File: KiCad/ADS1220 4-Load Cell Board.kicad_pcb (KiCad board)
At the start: 2 copper layers, 101.6 x 50.8 mm, 75 parts, among them J1 Conn_01x04, J2 Conn_01x04, J3 Conn_01x04, J4 Conn_ARM_SWD_TagConnect_TC203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, J5 USB_C_Receptacle_USB2.0_14P, J7 Conn_01x04, SW1 SW_Push, SW2 SW_Push, U1 STM32F103C8Tx, U2 ADS1220xPW, U3 MCP6V92-E/MS, U4 NCP1117-3.3_SOT223, U6 TLV702475_SOT23-5, Y1 8Mhz

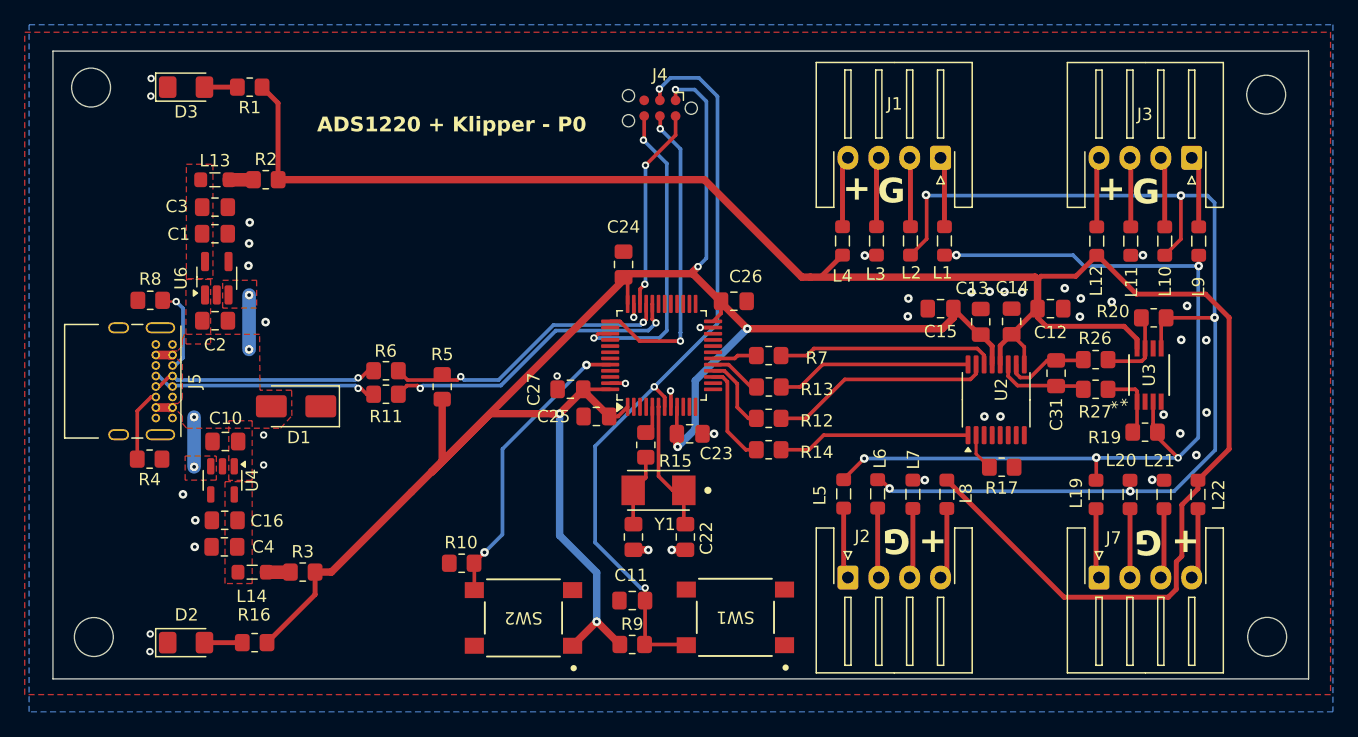
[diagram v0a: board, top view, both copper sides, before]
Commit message: Re-add Via Stitching
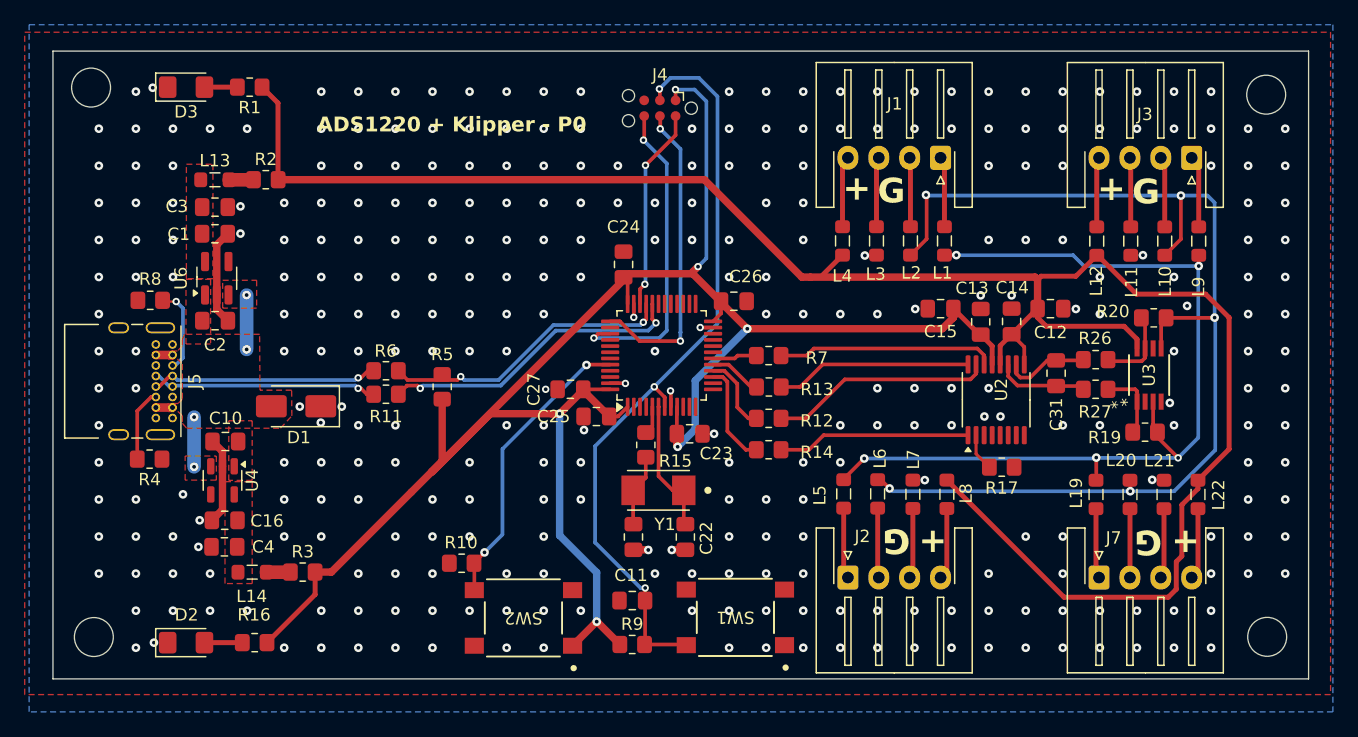
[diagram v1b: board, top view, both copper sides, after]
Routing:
- net GND: track 7.00 -> 21.8 mm, vias 44 -> 327

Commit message: Work In Progress
moving towards v 2
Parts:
- removed J4: Conn_ARM_SWD_TagConnect_TC2030-NL, Connector:Tag-Connect_TC2030-IDC-NL_2x03_P1.27mm_Vertical
- removed SW1, SW2: SW_Push, PTS645 Switch:SWITCH_43SMTR92LFS
- added C5: 10uF, Capacitor_SMD:C_0805_2012Metric_Pad1.18x1.45mm_HandSolder, F.Cu at (116.2, 100.2)
- added C6: 10uF, Capacitor_SMD:C_0805_2012Metric_Pad1.18x1.45mm_HandSolder, F.Cu at (114.2, 100.2)
- added C7: 0.1uF, Capacitor_SMD:C_0805_2012Metric_Pad1.18x1.45mm_HandSolder, F.Cu at (117.3, 95.9)
- added C8: 0.1uF, Capacitor_SMD:C_0805_2012Metric_Pad1.18x1.45mm_HandSolder, F.Cu at (117.3, 89.9)
- added D4: LED, LED_SMD:LED_1206_3216Metric_Pad1.42x1.75mm_HandSolder, F.Cu at (95.0, 72.3)
- added J6: Conn_01x02, Connector_PinHeader_2.54mm:PinHeader_1x02_P2.54mm_Vertical, F.Cu at (91.8, 116.9)
- added J8: Conn_01x02, Connector_PinHeader_2.54mm:PinHeader_1x02_P2.54mm_Vertical, F.Cu at (76.1, 117.0)
- added R18: 100R, Resistor_SMD:R_0805_2012Metric_Pad1.20x1.40mm_HandSolder, F.Cu at (119.1, 101.2)
- added R21: 100R, Resistor_SMD:R_0805_2012Metric_Pad1.20x1.40mm_HandSolder, F.Cu at (119.1, 99.2)
- added SWD_Header1: Conn_02x03_Counter_Clockwise, Connector_PinHeader_2.54mm:PinHeader_2x03_P2.54mm_Vertical, F.Cu at (83.1, 74.8)
- C21, C22: value 18pF -> 30pF
- C31: value 100n -> 0.1uF
- J1, J2, J3, J7: footprint Connector_JST:JST_XH_S4B-XH-A-1_1x04_P2.50mm_Horizontal -> Connector_JST:JST_XH_B4B-XH-A_1x04_P2.50mm_Vertical
- R15: value 1.1k -> 620R
- U1: footprint Package_QFP:LQFP-48_7x7mm_P0.5mm -> STM32F103C8T6TR:LQFP48_STM
- moved R15 26.8 mm to (95.0, 75.9), turned to 0 degrees
- moved R17 18.9 mm to (94.7, 103.4), turned to 0 degrees
- moved C26 11.5 mm to (80.8, 86.1), turned to -90 degrees
- moved C12 8.60 mm to (110.0, 93.9), turned to -90 degrees
- moved C13 6.91 mm to (106.4, 95.0), turned to 180 degrees
- moved C14 6.44 mm to (108.0, 91.7)
- moved R27 5.84 mm to (117.3, 91.9)
- moved C15 5.51 mm to (104.2, 93.0)
- moved U2 4.19 mm to (110.3, 100.1)
- moved C31 4.16 mm to (114.4, 92.9), turned to 90 degrees
- moved R26 3.93 mm to (117.3, 93.9)
- moved C21 1.28 mm to (83.8, 106.9)
- moved C22 1.28 mm to (88.0, 106.9)
- moved Y1 1.28 mm to (85.8, 103.1)
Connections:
- C21 pad 1: Net-(C21-Pad1) -> PD0
- J5 pad S1: GND -> Earth
- L11 pad 1: GND -> +4V
- L12 pad 1: +4V -> GND
- L21 pad 1: GND -> +4V
- L22 pad 1: +4V -> GND
- L3 pad 1: GND -> +4V
- L4 pad 1: +4V -> GND
- L7 pad 1: GND -> +4V
- L8 pad 1: +4V -> GND
- R15 pad 1: PD0 -> Net-(D4-A)
- R15 pad 2: Net-(C21-Pad1) -> Net-(U1-PB12)
- U1 pad 25: unconnected-(U1-PB12-Pad25) -> Net-(U1-PB12)
- U1 pad 39: SWO -> unconnected-(U1-PB3-Pad39)
- U2 pad 8: GND -> Net-(U2-REFN0)
- U2 pad 9: +4V -> Net-(U2-REFP0)
- Y1 pad 2: Net-(C21-Pad1) -> PD0
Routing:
- net NRESET: track 62.4 -> 30.1 mm, vias 3 -> 2
- net SWO: track 25.8 -> 0.00 mm, vias 2 -> 0
- net Net-(U1-PB12): track 0.00 -> 16.5 mm, vias 0 -> 2
- net Net-(U2-~{DRDY}): track 17.6 -> 9.78 mm
- net Net-(U2-DOUT/~{DRDY}): track 18.0 -> 10.2 mm
- net Net-(U2-SCLK): track 15.6 -> 7.82 mm
- net Net-(U2-DIN): track 15.9 -> 8.07 mm
- net Net-(U2-REFP0): track 0.00 -> 7.19 mm
- net Net-(U2-~{CS}): track 3.03 -> 10.00 mm
- net Net-(U2-REFN0): track 0.00 -> 6.95 mm
- net PD0: track 2.30 -> 8.82 mm
- net Net-(C21-Pad1): track 5.85 -> 0.00 mm
- net BOOT0: track 23.9 -> 29.3 mm
- net +3.3V: track 168.6 -> 164.4 mm, vias 6 -> 5
- net /ADS1220 AD Converter/AIN1: track 5.83 -> 1.90 mm
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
